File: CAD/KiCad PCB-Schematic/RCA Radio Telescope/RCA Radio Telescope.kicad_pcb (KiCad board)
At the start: 2 copper layers, 60 x 40 mm, 34 parts, among them J2 5V From PoE Splitter, J3 3V Out For LNA, J4 5V Out For Filter Board, J7 USB_A, J8 USB_A, Q1 DMP4047LFDE-7, U13 MAX8510ETA30+T, U14 TPS62133RGTR

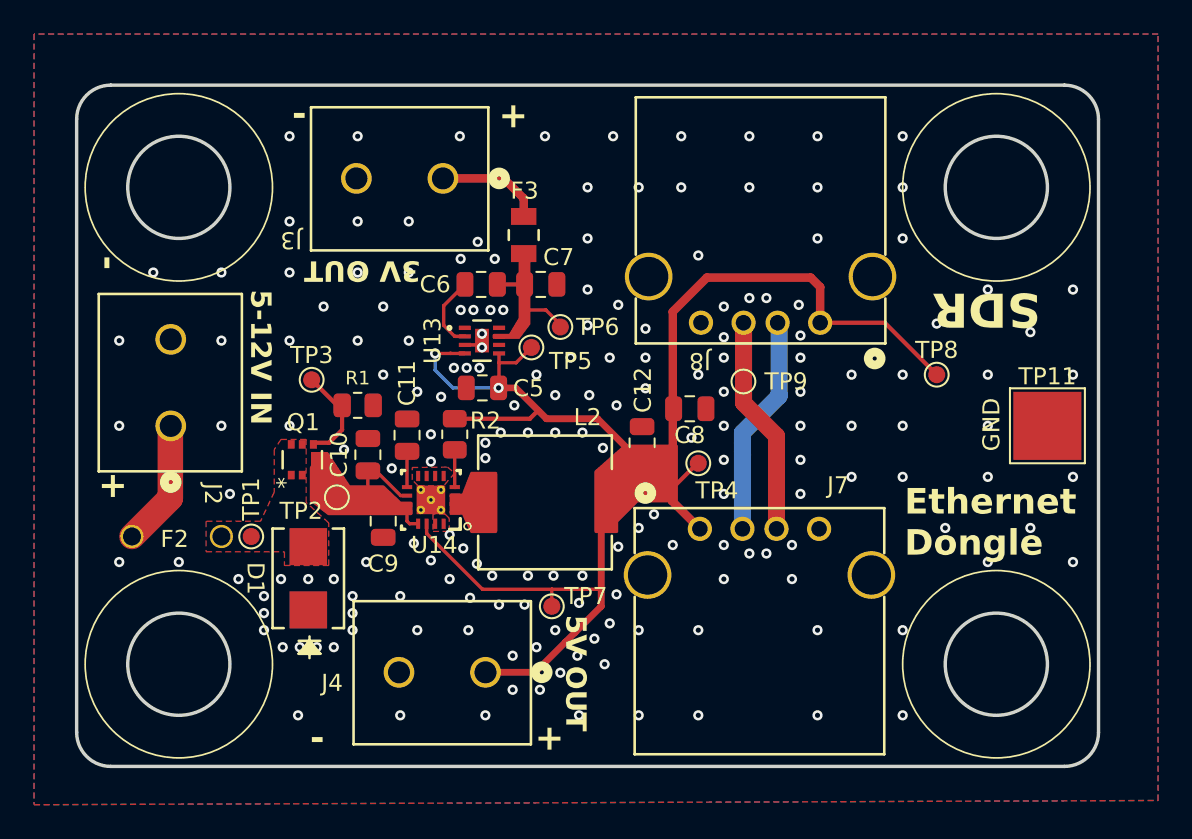
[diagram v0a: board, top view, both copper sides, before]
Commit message: Updated PowerData Schematic to v1.9 and PCB to v1.8
- Swapped LDO (Obsolete) with an Active version in both Schematic and PCB
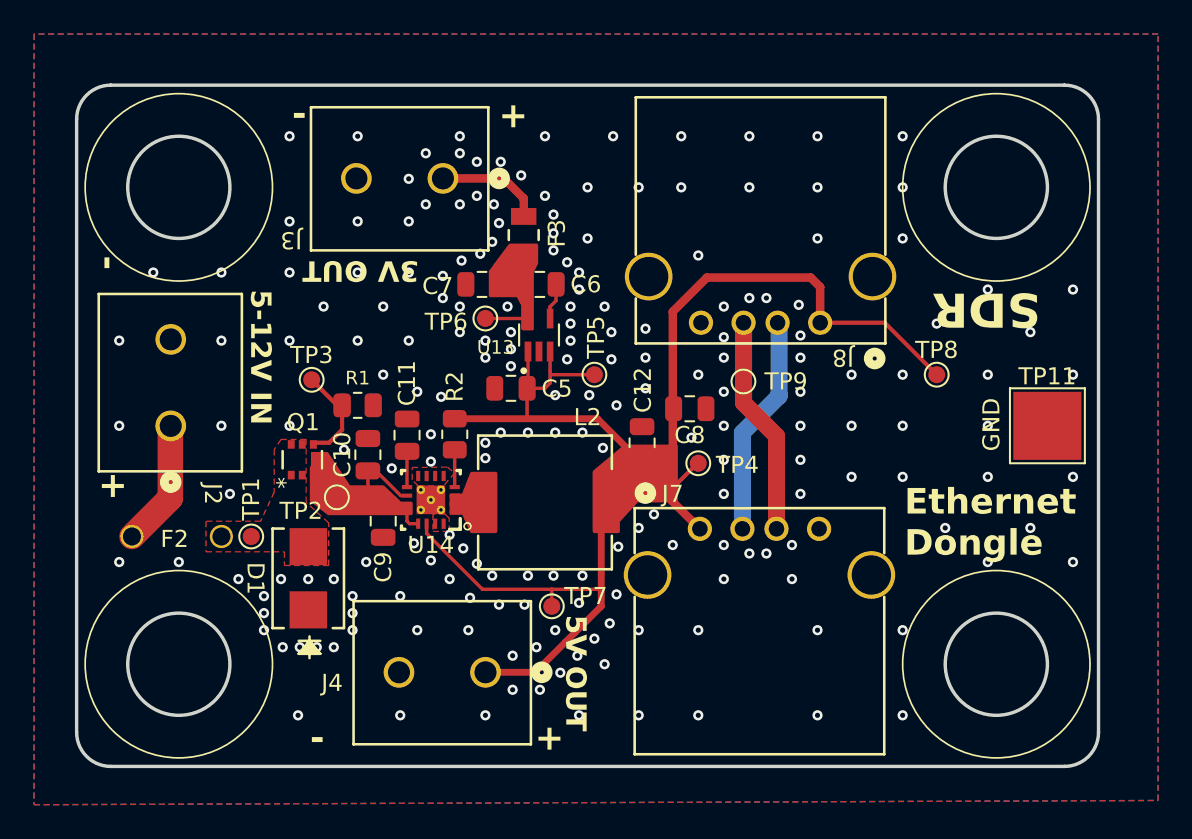
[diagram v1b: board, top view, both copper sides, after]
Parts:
- U13: value MAX8510ETA30+T -> MAX8510EXK30T; footprint Library:21-0168E_T822-1_MXM -> Library:SOT65P210X110-5N
- moved TP6 4.43 mm to (38.0, 27.7), turned to -90 degrees
- moved TP5 4.03 mm to (44.4, 31.0)
- moved C6 3.45 mm to (41.2, 25.7)
- moved C7 3.45 mm to (37.8, 25.7), turned to 180 degrees
- moved U13 3.37 mm to (41.1, 28.7), turned to 90 degrees
- moved C5 1.68 mm to (39.5, 31.8)
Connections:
- C6 pad 1: Net-(U13-BP) -> Net-(U13-OUT)
- C6 pad 2: Net-(U13-OUT) -> Net-(U13-BP)
- U13 pad 1: unconnected-(U13-NC-Pad1) -> +5V
- U13 pad 2: Net-(U13-BP) -> GND
- U13 pad 3: GND -> +5V
- U13 pad 4: +5V -> Net-(U13-BP)
- U13 pad 5: +5V -> Net-(U13-OUT)
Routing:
- net +5V: track 89.9 -> 85.5 mm, vias 2 -> 0
- net Net-(U13-BP): track 4.43 -> 2.14 mm
- net Net-(U13-OUT): track 3.80 -> 2.50 mm
- net GND: track 1.11 -> 0.00 mm, vias 181 -> 200
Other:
- board text added: "PSU ECE Capstone Team 11 - RCA Telescope v1.8 (3/27/2025)"
- board text removed: "PSU ECE Capstone Team 11 - RCA Telescope v1.7 (3/27/2025)"
